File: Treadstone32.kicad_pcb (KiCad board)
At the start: 2 copper layers, 198.8 x 75.8 mm, 84 parts, among them SW1 SW_DIP_x01, SW10 SW_PUSH, SW11 SW_PUSH, SW12 SW_PUSH, SW13 SW_PUSH, SW14 SW_PUSH, SW15 SW_PUSH, SW16 SW_PUSH, SW17 SW_PUSH, SW18 SW_PUSH, SW19 SW_PUSH, SW2 SW_PUSH, SW20 SW_PUSH, SW21 SW_PUSH, SW22 SW_PUSH, SW23 SW_PUSH, SW24 SW_PUSH, SW25 SW_PUSH, SW26 SW_PUSH, SW27 SW_PUSH, SW28 SW_PUSH, SW29 SW_PUSH, SW3 SW_PUSH, SW30 SW_PUSH, SW31 SW_PUSH, SW32 SW_PUSH, SW33 SW_PUSH, SW4 SW_PUSH, SW5 SW_PUSH, SW6 SW_PUSH, SW7 SW_PUSH, SW8 SW_PUSH, SW9 SW_PUSH, U1 ATmega32U4-AU, X1 16MHz

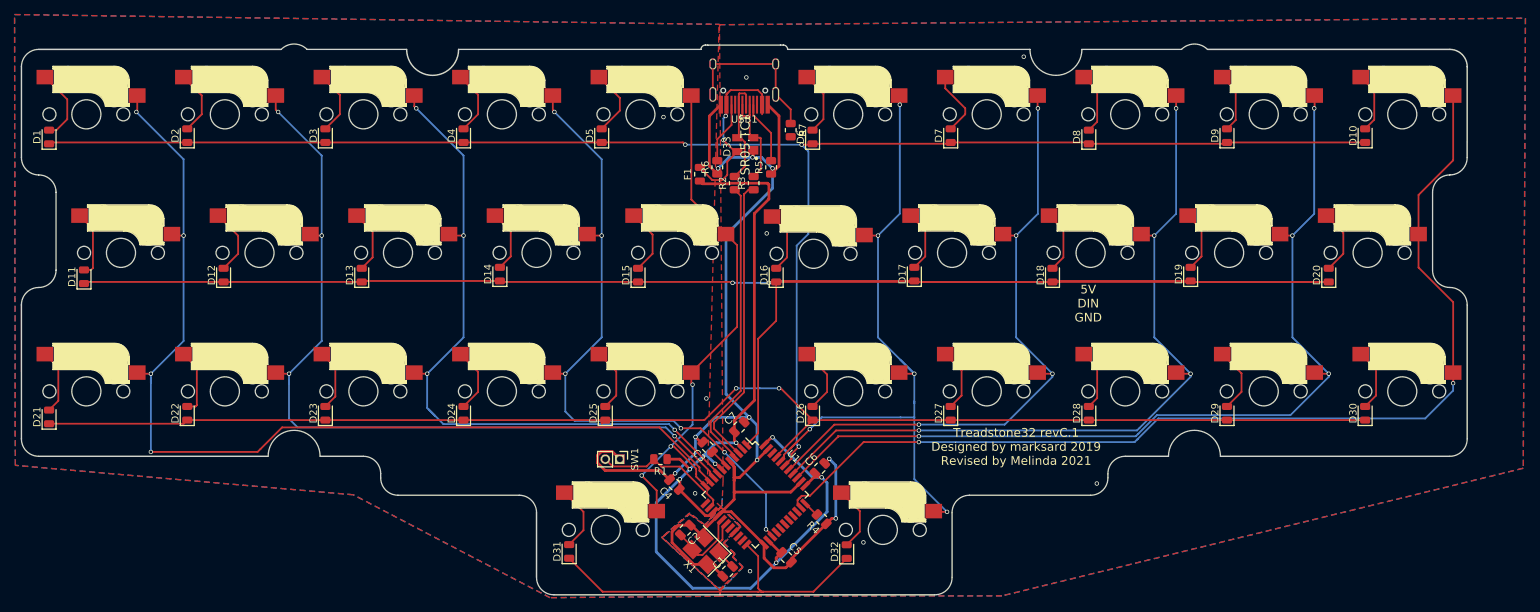
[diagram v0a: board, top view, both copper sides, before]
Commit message: Add underglow and switch to solderable switches
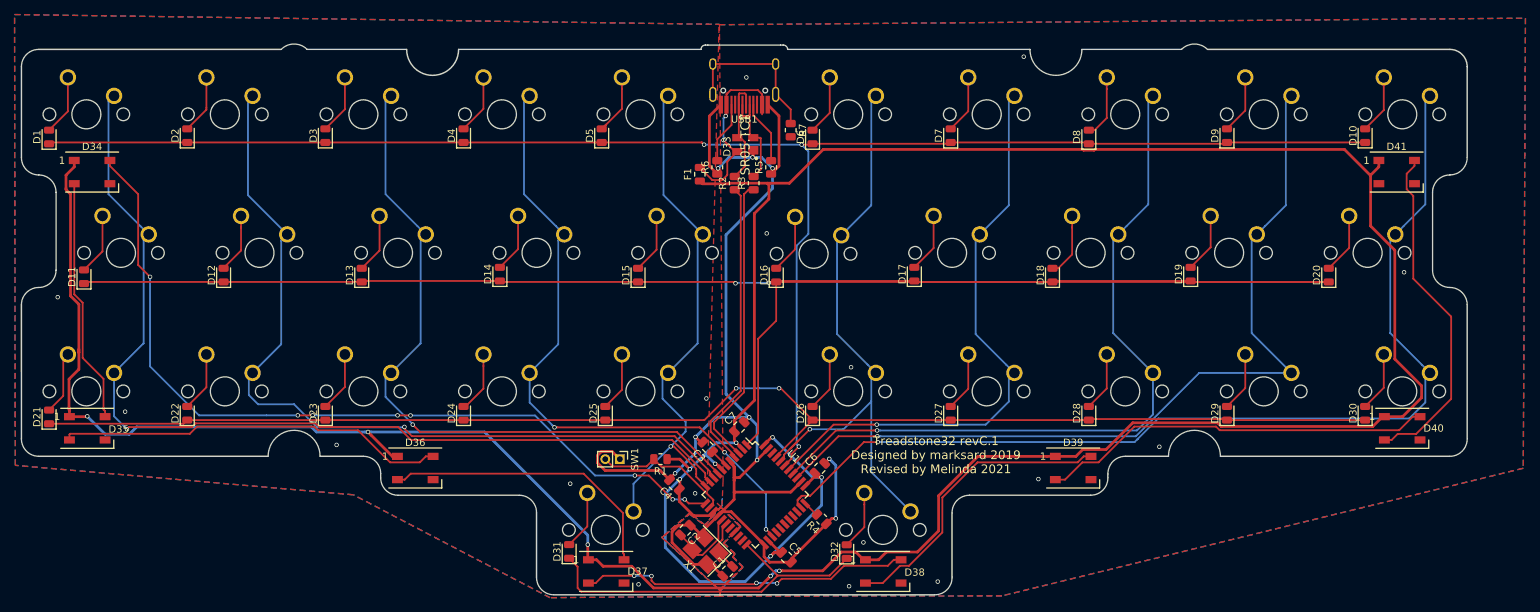
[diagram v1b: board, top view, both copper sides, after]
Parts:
- added D34: WS2812B, LED_SMD:LED_WS2812B_PLCC4_5.0x5.0mm_P3.2mm, F.Cu at (110.9, 75.1)
- added D35: WS2812B, LED_SMD:LED_WS2812B_PLCC4_5.0x5.0mm_P3.2mm, F.Cu at (110.2, 110.4)
- added D36: WS2812B, LED_SMD:LED_WS2812B_PLCC4_5.0x5.0mm_P3.2mm, F.Cu at (155.3, 115.8)
- added D37: WS2812B, LED_SMD:LED_WS2812B_PLCC4_5.0x5.0mm_P3.2mm, F.Cu at (181.6, 130.1)
- added D38: WS2812B, LED_SMD:LED_WS2812B_PLCC4_5.0x5.0mm_P3.2mm, F.Cu at (219.7, 130.1)
- added D39: WS2812B, LED_SMD:LED_WS2812B_PLCC4_5.0x5.0mm_P3.2mm, F.Cu at (245.8, 115.8)
- added D40: WS2812B, LED_SMD:LED_WS2812B_PLCC4_5.0x5.0mm_P3.2mm, F.Cu at (291.0, 110.4)
- added D41: WS2812B, LED_SMD:LED_WS2812B_PLCC4_5.0x5.0mm_P3.2mm, F.Cu at (290.3, 75.1)
- SW10, SW11, SW12, SW13, SW14, SW15, SW16, SW17, SW18, SW19, SW2, SW20, SW21, SW22, SW23, SW24, SW25, SW26, SW27, SW28, SW29, SW3, SW30, SW31, SW32, SW33, SW4, SW5, SW6, SW7, SW8, SW9: footprint kbd:CherryMX_Hotswap_front -> kbd:MXOnly-1U-NoLED; moved to B.Cu
- turned SW10 to 180 degrees
- turned SW11 to 180 degrees
- turned SW12 to 180 degrees
- turned SW13 to 180 degrees
- turned SW14 to 180 degrees
- turned SW15 to 180 degrees
- turned SW16 to 180 degrees
- turned SW17 to 180 degrees
- turned SW18 to 180 degrees
- turned SW19 to 180 degrees
- turned SW2 to 180 degrees
- turned SW20 to 180 degrees
- turned SW21 to 180 degrees
- turned SW22 to 180 degrees
- turned SW23 to 180 degrees
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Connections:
- U1 pad 12: Net-(U1-Pad12) -> RGB
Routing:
- net +5V: track 138.0 -> 513.4 mm, vias 7 -> 12
- net RGB: track 0.00 -> 114.8 mm, vias 0 -> 8
- net Net-(D39-Pad2): track 0.00 -> 54.2 mm
- net Net-(D35-Pad2): track 0.00 -> 53.6 mm
- net Net-(D40-Pad2): track 0.00 -> 47.3 mm
- net Net-(D37-Pad2): track 0.00 -> 45.7 mm, vias 0 -> 4
- net Net-(D38-Pad2): track 0.00 -> 41.0 mm
- net Net-(D36-Pad2): track 0.00 -> 40.1 mm
- net Net-(D34-Pad2): track 0.00 -> 33.8 mm
- net col5: track 94.0 -> 81.6 mm, vias 5 -> 1
- net col8: track 124.7 -> 116.6 mm, vias 4 -> 1
- net col6: track 87.6 -> 80.9 mm, vias 4 -> 1
- net col7: track 106.1 -> 101.2 mm, vias 4 -> 1
- net col0: track 139.5 -> 135.3 mm, vias 4 -> 1
- net col9: track 143.1 -> 141.0 mm, vias 2 -> 1
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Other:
- board text removed: "5V DIN GND"
